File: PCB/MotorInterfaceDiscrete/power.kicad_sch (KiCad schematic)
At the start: 3 parts, among them U2 74LS14, U3 74LS08, U5 74LS76

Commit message: cleanup and rename
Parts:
- renumbered U5 to U2, U2 to U3, U3 to U4
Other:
- title: (none) -> Motor Interface - Discrete Logic
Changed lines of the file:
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@@
 (kicad_sch (version 20230121) (generator eeschema)
-  (paper "A4")
+  (paper "USLetter")
+  (title_block
+    (title "Motor Interface - Discrete Logic")
+    (date "2024-05-22")
+    (rev "1")
+  )
   (junction (at 55.88 76.2) (diameter 0) (color 0 0 0 0)
   )
@@
   (symbol (lib_id "F2018-cache:GND") (at 46.99 76.2 0) (unit 1)
     (in_bom yes) (on_board yes) (dnp no) (fields_autoplaced)
-    (property "Reference" "#PWR03" (at 46.99 82.55 0)
+    (property "Reference" "#PWR014" (at 46.99 82.55 0)
       (effects (font (size 1.27 1.27)) hide)
     )
@@
       (project "MotorInterface"
         (path "/18987dfd-1111-4fcd-8666-686e24f32049/09eca958-6e6a-489b-8565-6fc4aa47d77e"
-          (reference "#PWR03") (unit 1)
+          (reference "#PWR014") (unit 1)
         )
       )
@@
   (symbol (lib_id "00TJR:74xx_74LS76") (at 95.25 58.42 0) (unit 3)
     (in_bom yes) (on_board yes) (dnp no)
-    (property "Reference" "U5" (at 88.9 52.07 0)
+    (property "Reference" "U2" (at 88.9 52.07 0)
       (effects (font (size 1.27 1.27)) (justify left))
     )
@@
       (project "MotorInterface"
         (path "/18987dfd-1111-4fcd-8666-686e24f32049/09eca958-6e6a-489b-8565-6fc4aa47d77e"
-          (reference "U5") (unit 3)
+          (reference "U2") (unit 3)
         )
       )
@@
   (symbol (lib_id "S2020-cache:74xx_74LS14") (at 55.88 60.96 0) (unit 7)
     (in_bom yes) (on_board yes) (dnp no)
-    (property "Reference" "U2" (at 50.8 52.07 0)
+    (property "Reference" "U3" (at 50.8 52.07 0)
       (effects (font (size 1.27 1.27)))
     )
@@
       (project "MotorInterface"
         (path "/18987dfd-1111-4fcd-8666-686e24f32049/09eca958-6e6a-489b-8565-6fc4aa47d77e"
-          (reference "U2") (unit 7)
+          (reference "U3") (unit 7)
         )
       )
@@
   (symbol (lib_id "BJT-Amps-cache:power_VCC") (at 46.99 45.72 0) (unit 1)
     (in_bom yes) (on_board yes) (dnp no) (fields_autoplaced)
-    (property "Reference" "#PWR01" (at 46.99 49.53 0)
+    (property "Reference" "#PWR013" (at 46.99 49.53 0)
       (effects (font (size 1.27 1.27)) hide)
     )
@@
       (project "MotorInterface"
         (path "/18987dfd-1111-4fcd-8666-686e24f32049/09eca958-6e6a-489b-8565-6fc4aa47d77e"
-          (reference "#PWR01") (unit 1)
+          (reference "#PWR013") (unit 1)
         )
       )
@@
   (symbol (lib_id "TFlipFlop-cache:74xx_74LS08") (at 76.2 60.96 0) (mirror y) (unit 5)
     (in_bom yes) (on_board yes) (dnp no)
-    (property "Reference" "U3" (at 69.85 52.07 0)
+    (property "Reference" "U4" (at 69.85 52.07 0)
       (effects (font (size 1.27 1.27)))
     )
@@
       (project "MotorInterface"
         (path "/18987dfd-1111-4fcd-8666-686e24f32049/09eca958-6e6a-489b-8565-6fc4aa47d77e"
-          (reference "U3") (unit 5)
-        )
-      )
+          (reference "U4") (unit 5)
+        )
+      )

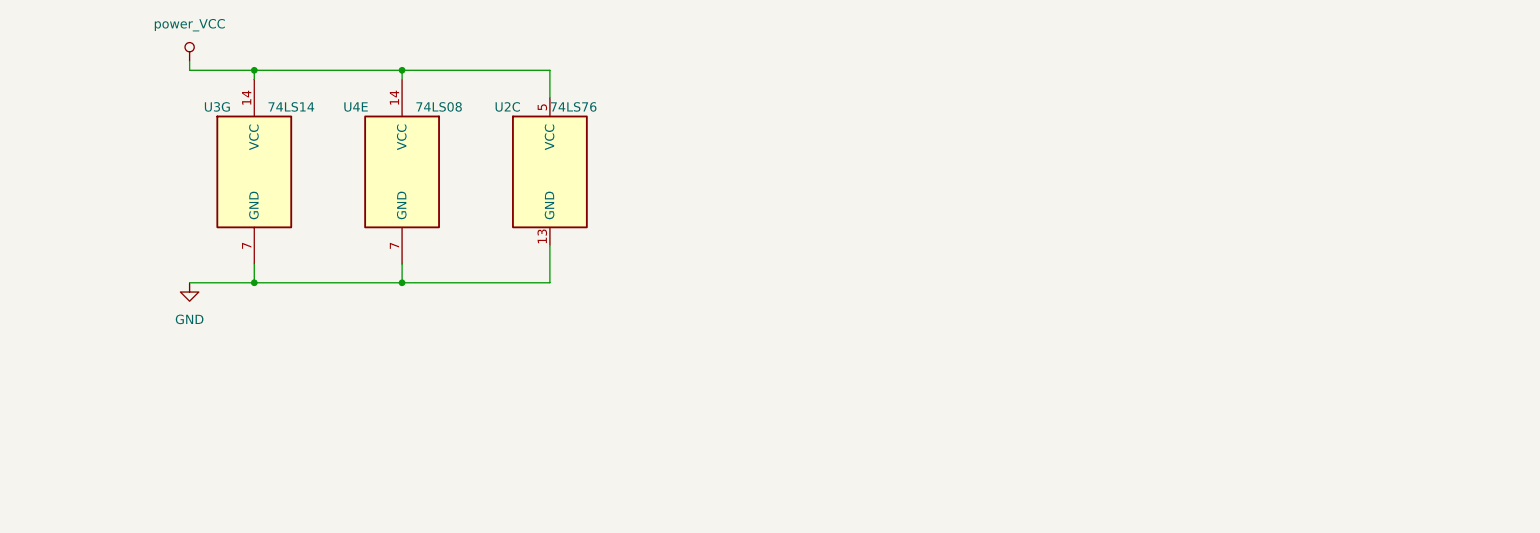
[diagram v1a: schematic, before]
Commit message: update symbols, add decouple
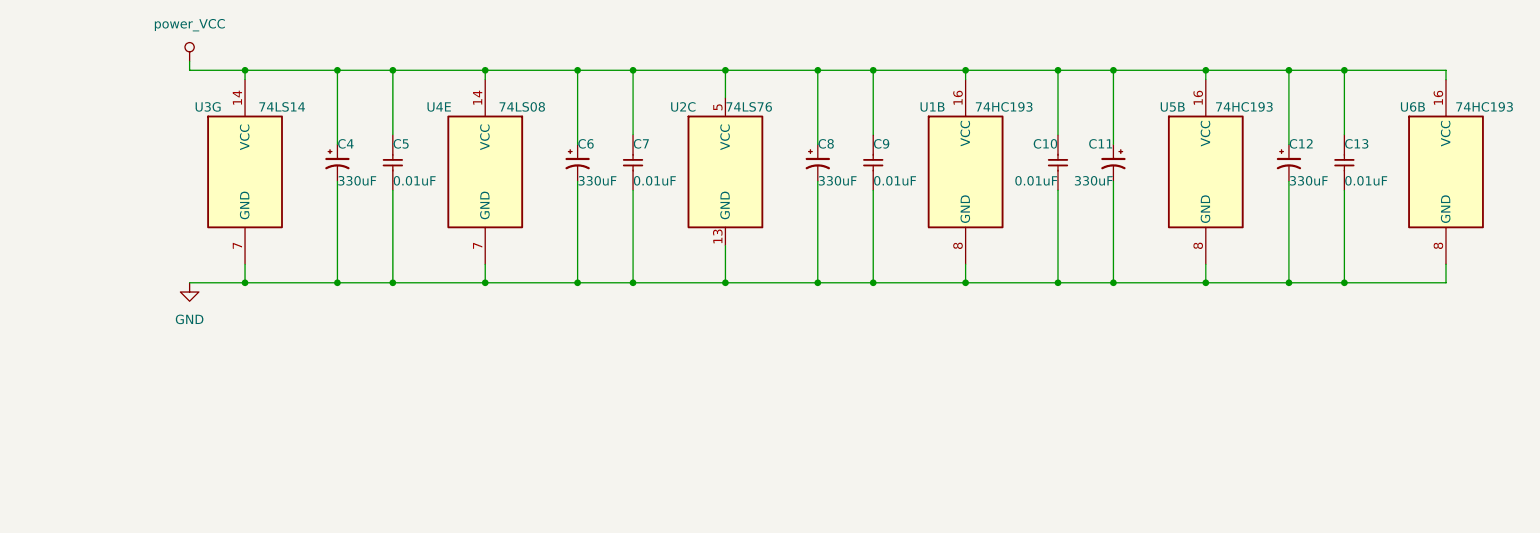
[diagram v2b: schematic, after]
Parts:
- added C10, C13, C5, C7, C9: 0.01uF, symbol 00TJR:C_small
- added C11, C12, C4, C6, C8: 330uF, symbol 00TJR:CP1_Small
- added U1, U5, U6: 74HC193, symbol 00TJR:74HC193
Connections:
- net GND: now also C10.2, C11.2, C12.2, C13.2, C4.2, C5.2, C6.2, C7.2, C8.2, C9.2, U1.8 (GND), U5.8 (GND), U6.8 (GND)
- net VCC: now also C10.1, C11.1, C12.1, C13.1, C4.1, C5.1, C6.1, C7.1, C8.1, C9.1, U1.16 (VCC), U5.16 (VCC), U6.16 (VCC)
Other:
- moved on the sheet: U2C, U3G, U4E

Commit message: add tested analog speed circuit
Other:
- note added: "Analog voltage will be 0v to the value. Expect 10V to 12V"
